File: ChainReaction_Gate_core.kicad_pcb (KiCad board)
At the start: 2 copper layers, 38.1 x 99.1 mm, 48 parts, among them J18 conn_L, J19 conn_R, J20 power_bus, U4 4017, U5 TL072, U6 4013, U7 TL074

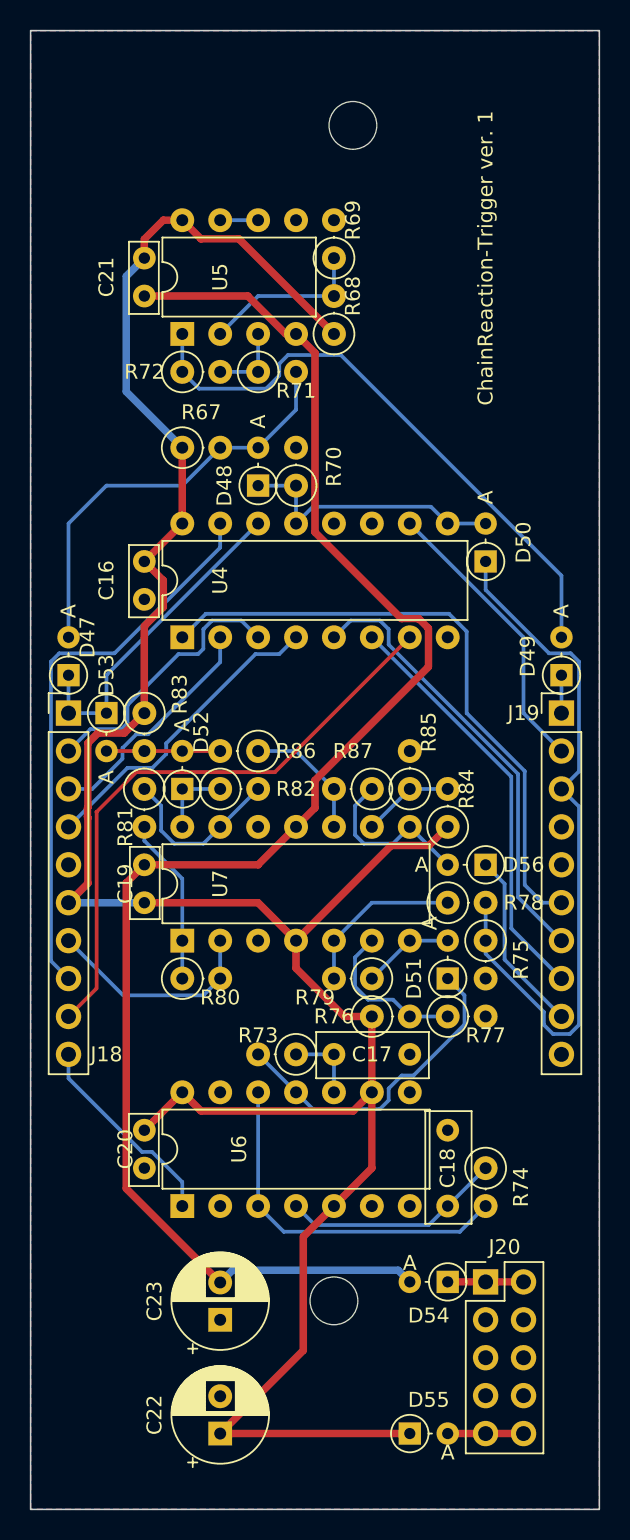
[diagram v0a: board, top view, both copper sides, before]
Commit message: Fixed problems: - added power-on reset function - added 100ks to discharge caps with FFs(4013) - only for the CV; adjusted the parameter (100k -> 10k) of a resistor with a FF
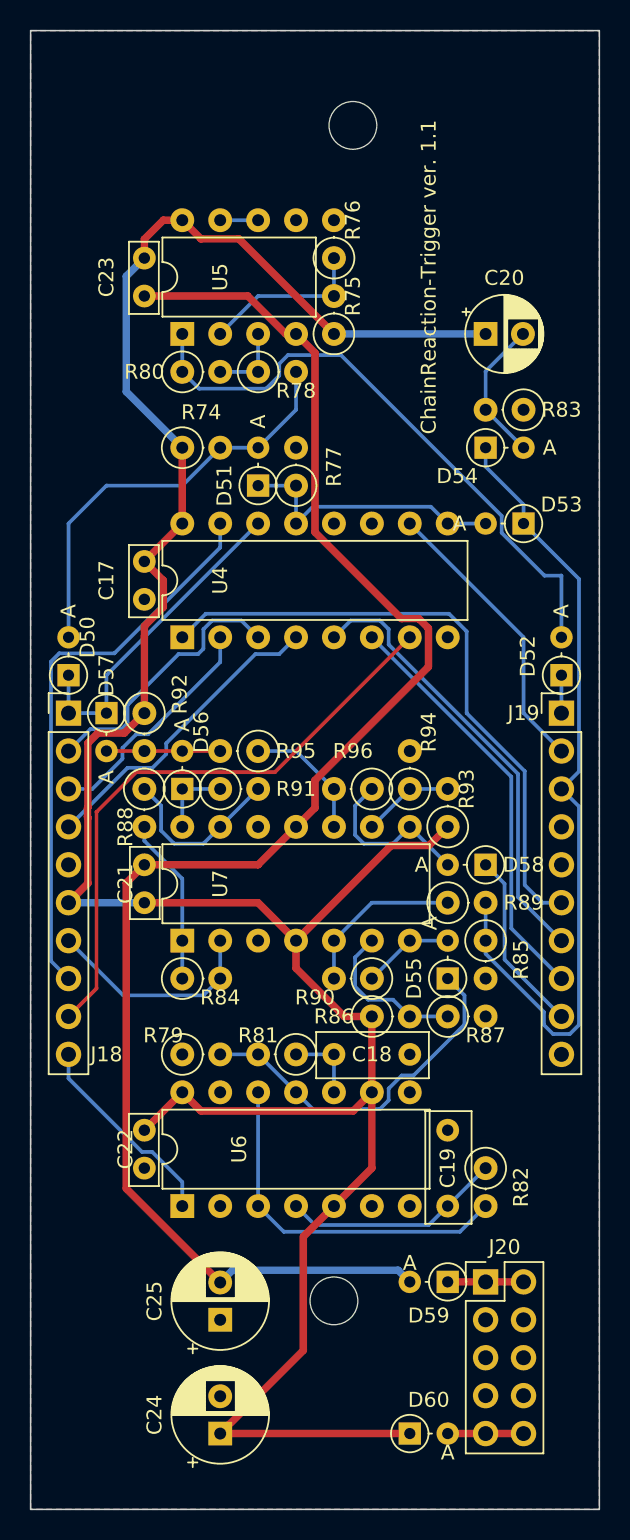
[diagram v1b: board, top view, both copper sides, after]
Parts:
- added C20: 1u, Capacitor_THT:CP_Radial_D5.0mm_P2.50mm, F.Cu at (94.0, 58.4)
- added D54: D, Diode_THT:D_DO-34_SOD68_P2.54mm_Vertical_AnodeUp, F.Cu at (94.0, 66.0)
- added R79: 10k, Resistor_THT:R_Axial_DIN0207_L6.3mm_D2.5mm_P2.54mm_Vertical, F.Cu at (73.7, 106.7)
- added R83: 1M, Resistor_THT:R_Axial_DIN0207_L6.3mm_D2.5mm_P2.54mm_Vertical, F.Cu at (96.5, 63.5)
- moved D53 3.59 mm to (96.5, 71.1), turned to 180 degrees
- renumbered C16 to C17, C17 to C18, C18 to C19, C19 to C21, C20 to C22, C21 to C23, C22 to C24, C23 to C25, D47 to D50, D48 to D51, D49 to D52, D50 to D53, D51 to D55, D52 to D56, D53 to D57, D56 to D58, D54 to D59, D55 to D60, R67 to R74, R68 to R75, R69 to R76, R70 to R77, R71 to R78, R72 to R80, R73 to R81, R74 to R82, R80 to R84, R75 to R85, R76 to R86, R77 to R87, R81 to R88, R78 to R89, R79 to R90, R82 to R91, R83 to R92, R84 to R93, R85 to R94, R86 to R95, R87 to R96
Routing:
- net +12V: track 168.2 -> 178.4 mm
- net Net-(C20-Pad2): track 0.00 -> 9.71 mm
- net /Trigger_Logic/stop: track 48.1 -> 54.9 mm
- net /Trigger_Logic/EoC_in: track 21.7 -> 24.2 mm
- net Net-(D52-Pad2): track 40.1 -> 40.7 mm
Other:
- board text added: "ChainReaction-Trigger ver. 1.1"
- board text removed: "ChainReaction-Trigger ver. 1"
